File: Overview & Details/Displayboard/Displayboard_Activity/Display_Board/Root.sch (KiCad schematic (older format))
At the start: 38 parts, among them J1 Micro_SD_Card_Det_MOD-Connect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, J2 Conn_01x20_Female, J3 Conn_01x50-Connector_Generic, J4 Conn_01x20_Female, Q1 MMBT2222A-TP-dk_Transistors-B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, U1 MCP130T-300I_TT-dk_PMIC-Super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, U2 SN74LVC245AN-dk_Logic-Buffers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, U3 STMPE811QTR-Interface_Expansi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, U4 SN74LVC245AN-dk_Logic-Buffers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, U5 LP2988-3.3_SOIC8_VSSOP8

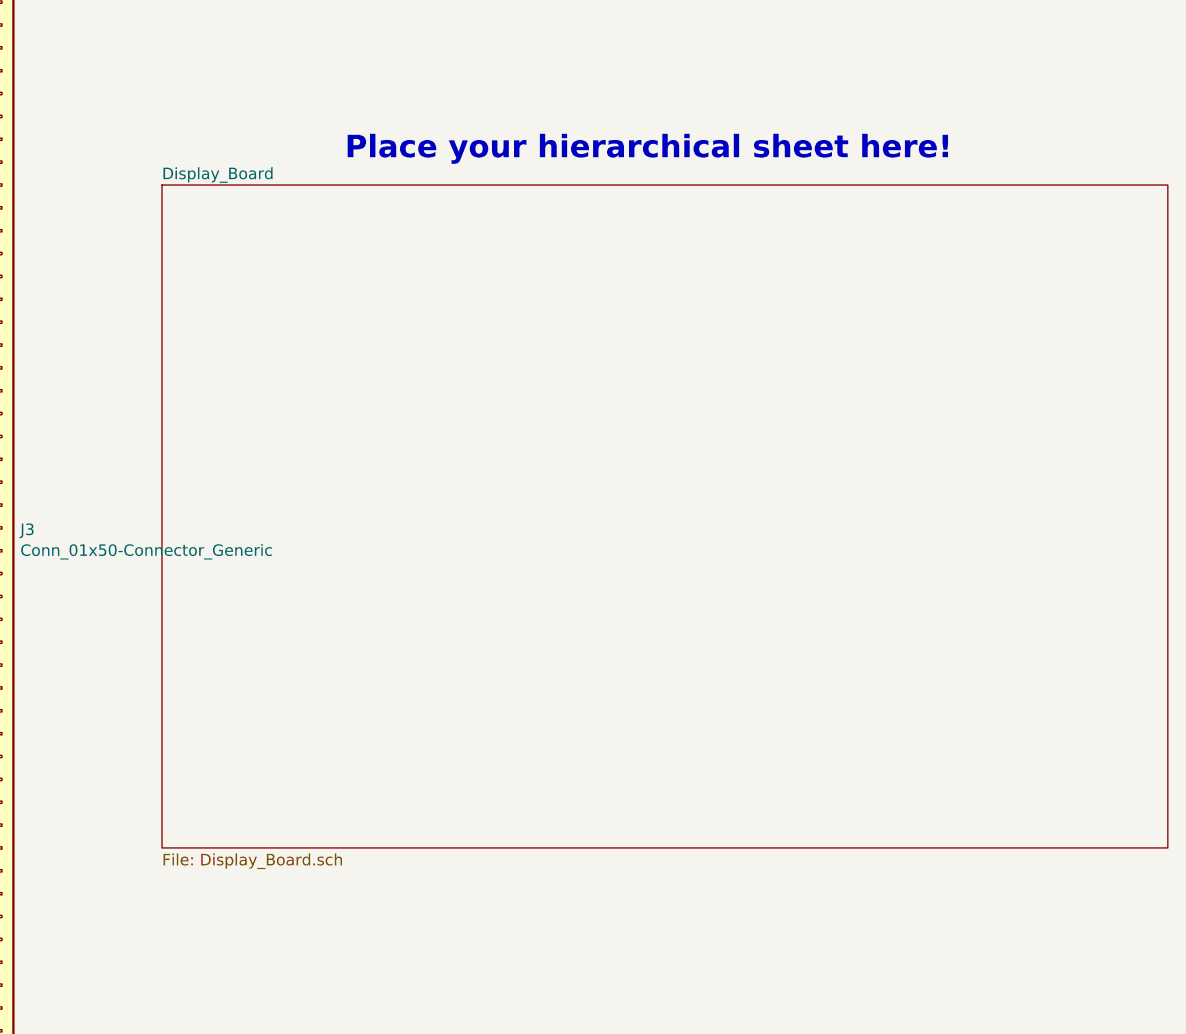
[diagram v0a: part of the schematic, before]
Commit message: Oops removed hierarchical sheet
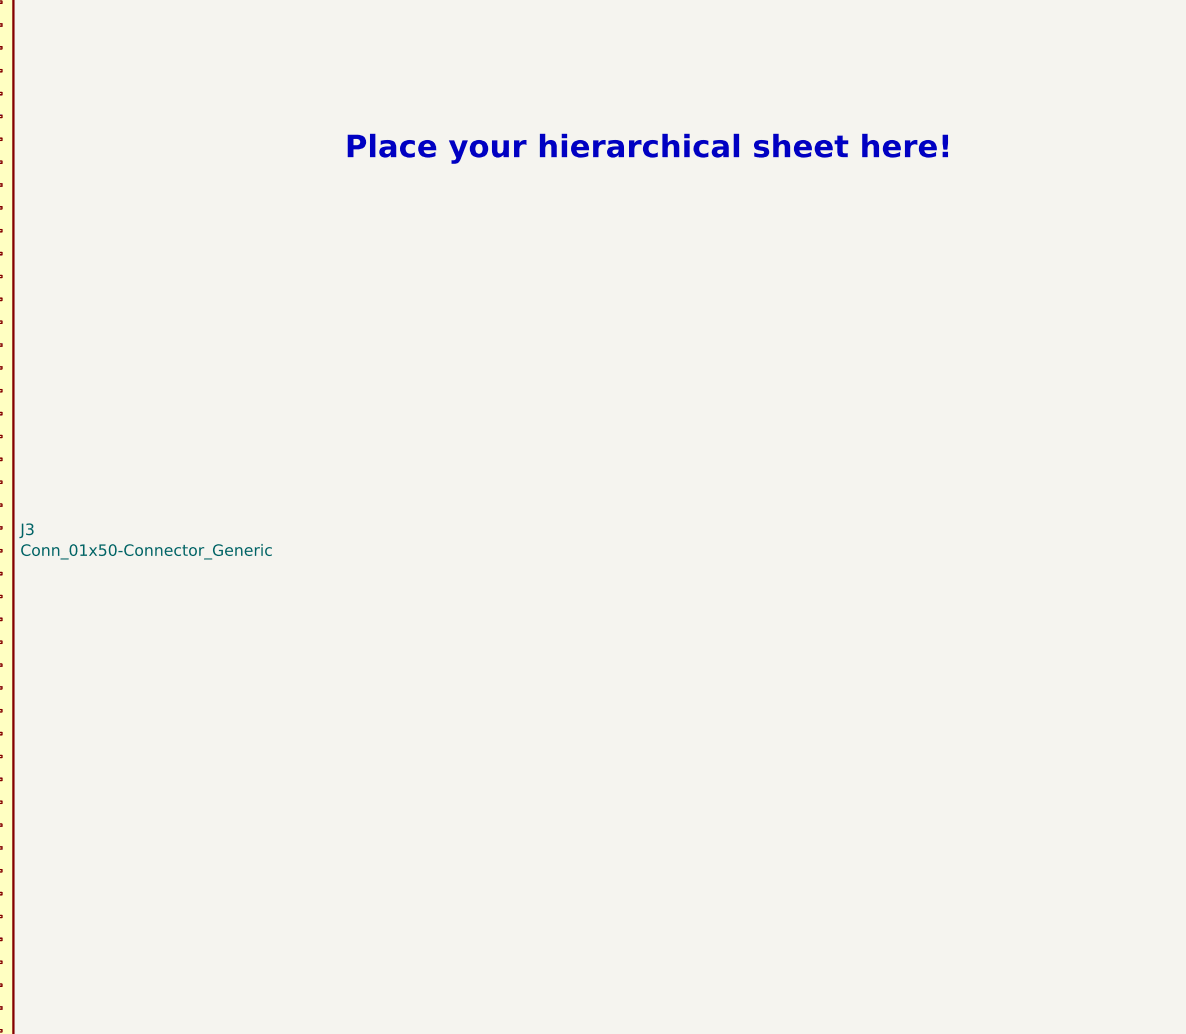
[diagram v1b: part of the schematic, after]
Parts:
- Q1, U1: footprint (none) -> Display_Board:SOT-23-3
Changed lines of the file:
@@
 $Descr B 17000 11000
 encoding utf-8
-Sheet 1 2
+Sheet 1 1
 Title "UberRadio Display Board"
 Date ""
@@
 F 0 "U1" H 4893 7413 60  0000 R CNN
 F 1 "MCP130T-300I_TT-dk_PMIC-Supervisors" H 4893 7307 60  0000 R CNN
-F 2 "" H 5220 7510 60  0001 L CNN
+F 2 "Display_Board:SOT-23-3" H 5220 7510 60  0001 L CNN
 F 3 "http://www.microchip.com/mymicrochip/filehandler.aspx?ddocname=en011325" H 5220 7610 60  0001 L CNN
 F 4 "MCP130T-300I/TTCT-ND" H 5220 7710 60  0001 L CNN "Digi-Key_PN"
@@
 F 0 "Q1" H 9788 2198 60  0000 L CNN
 F 1 "MMBT2222A-TP-dk_Transistors-Bipolar-BJT-Single" H 9788 2092 60  0000 L CNN
-F 2 "" H 9800 2345 60  0001 L CNN
+F 2 "Display_Board:SOT-23-3" H 9800 2345 60  0001 L CNN
 F 3 "http://www.mccsemi.com/up_pdf/MMBT2222A(SOT-23).pdf" H 9800 2445 60  0001 L CNN
 F 4 "MMBT2222ATPMSCT-ND" H 9800 2545 60  0001 L CNN "Digi-Key_PN"
@@
 Text Notes 12650 3750 0    98   ~ 20
 Place your hierarchical sheet here!
-$Sheet
-S 11850 3850 4400 2900
-U 5ED1B308
-F0 "Display_Board" 50
-F1 "Display_Board.sch" 50
-$EndSheet
 $EndSCHEMATC

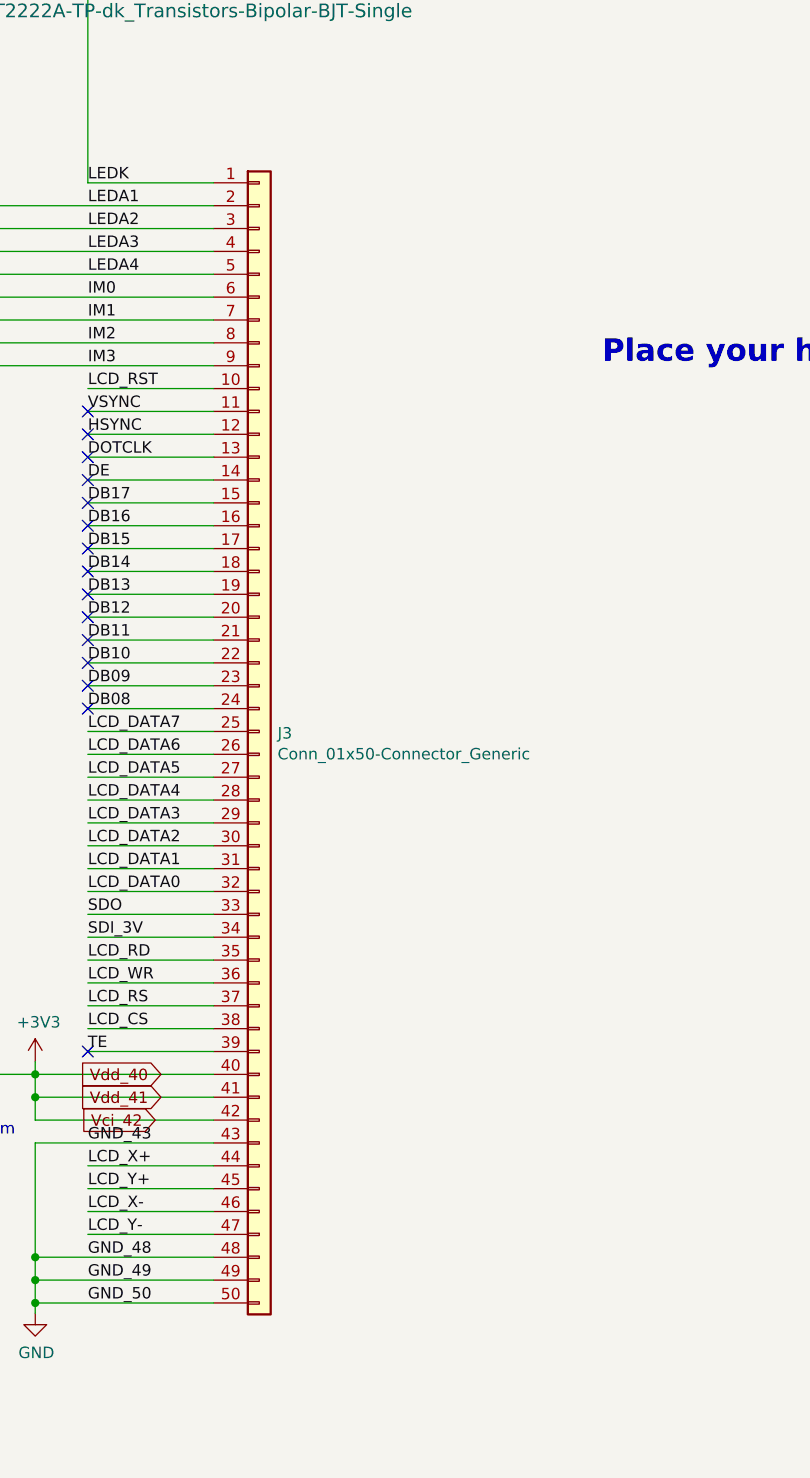
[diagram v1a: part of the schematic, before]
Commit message: Updated with Marion's footprints
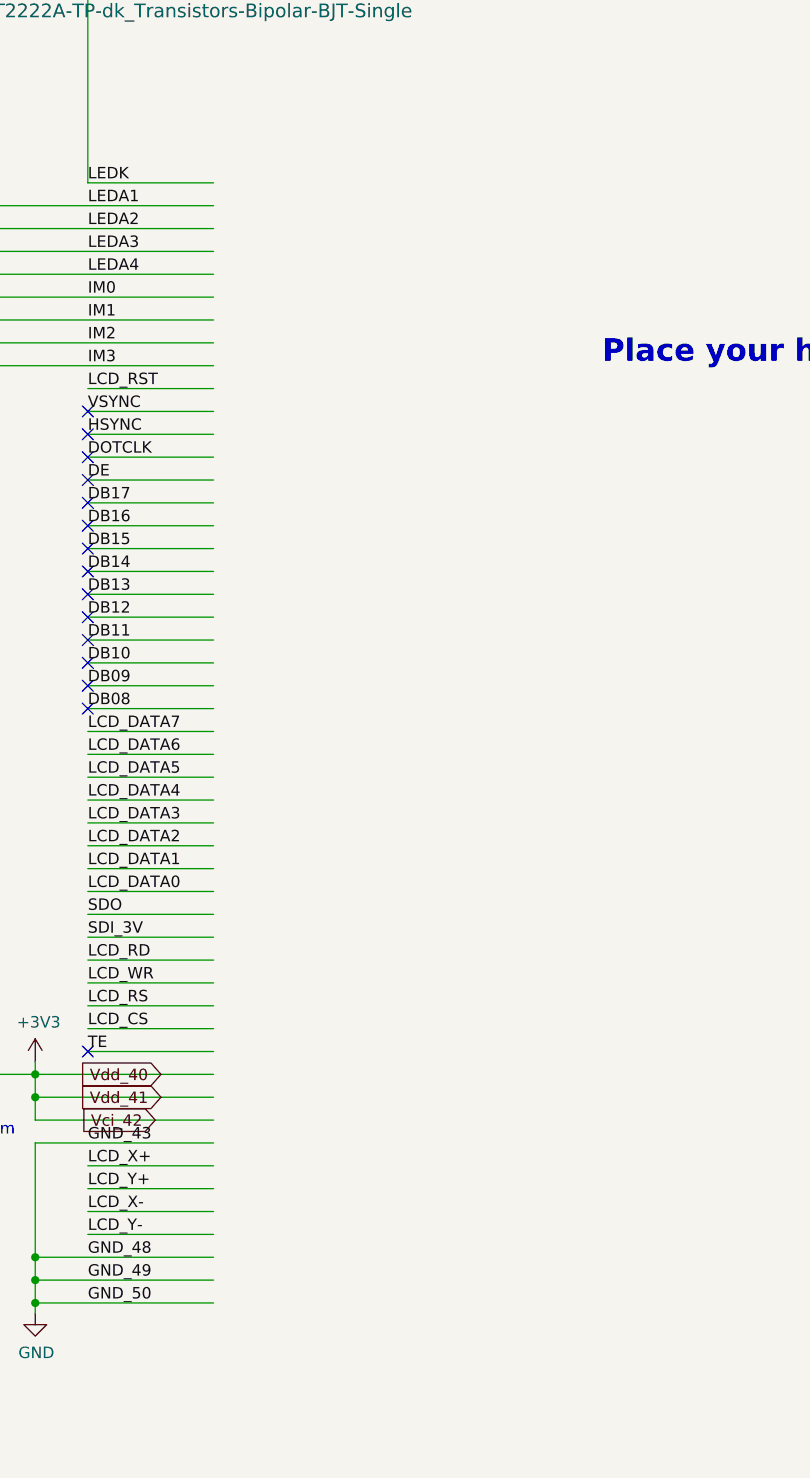
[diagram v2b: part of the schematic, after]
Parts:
- removed J3: Conn_01x50-Connector_Generic, Connector_FFC-FPC:TE_5-1734839-0_1x50-1MP_P0.5mm_Horizontal, symbol Display_Board:Conn_01x50-Connector_Generic
- J2, J4: footprint Connector_PinHeader_2.54mm:PinHeader_1x20_P2.54mm_Vertical -> Display_Board:1X20_ROUND
- JP1, JP2, JP3, JP4: footprint Jumper:SolderJumper-2_P1.3mm_Open_TrianglePad1.0x1.5mm -> Display_Board:SOLDERJUMPER_ARROW_NOPASTE
- U2, U4: footprint (none) -> Display_Board:SN74LVC245ARGYR
- U3: footprint Package_DFN_QFN:QFN-12-1EP_3x3mm_P0.51mm_EP1.45x1.45mm -> Display_Board:STMPE811
- U5: footprint Package_SO:SOIC-8_3.9x4.9mm_P1.27mm -> Display_Board:LP2988IMM-3.3_slash_NOPB
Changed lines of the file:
@@
 F 0 "JP2" V 7950 2860 50  0000 R CNN
 F 1 "SolderJumper_2_Open" V 7805 2822 50  0001 R CNN
-F 2 "Jumper:SolderJumper-2_P1.3mm_Open_TrianglePad1.0x1.5mm" H 7850 2910 50  0001 C CNN
+F 2 "Display_Board:SOLDERJUMPER_ARROW_NOPASTE" H 7850 2910 50  0001 C CNN
 F 3 "~" H 7850 2910 50  0001 C CNN
 	1    7850 2910
@@
 F 0 "JP1" V 7700 2860 50  0000 R CNN
 F 1 "SolderJumper_2_Open" V 7555 2822 50  0001 R CNN
-F 2 "Jumper:SolderJumper-2_P1.3mm_Open_TrianglePad1.0x1.5mm" H 7600 2910 50  0001 C CNN
+F 2 "Display_Board:SOLDERJUMPER_ARROW_NOPASTE" H 7600 2910 50  0001 C CNN
 F 3 "~" H 7600 2910 50  0001 C CNN
 	1    7600 2910
@@
 F 0 "JP3" V 8200 2860 50  0000 R CNN
 F 1 "SolderJumper_2_Open" V 8055 2822 50  0001 R CNN
-F 2 "Jumper:SolderJumper-2_P1.3mm_Open_TrianglePad1.0x1.5mm" H 8100 2910 50  0001 C CNN
+F 2 "Display_Board:SOLDERJUMPER_ARROW_NOPASTE" H 8100 2910 50  0001 C CNN
 F 3 "~" H 8100 2910 50  0001 C CNN
 	1    8100 2910
@@
 F 0 "JP4" V 8450 2860 50  0000 R CNN
 F 1 "SolderJumper_2_Open" V 8305 2822 50  0001 R CNN
-F 2 "Jumper:SolderJumper-2_P1.3mm_Open_TrianglePad1.0x1.5mm" H 8350 2910 50  0001 C CNN
+F 2 "Display_Board:SOLDERJUMPER_ARROW_NOPASTE" H 8350 2910 50  0001 C CNN
 F 3 "~" H 8350 2910 50  0001 C CNN
 	1    8350 2910
@@
 F 0 "U5" H 5280 9522 50  0000 C CNN
 F 1 "LP2988-3.3_SOIC8_VSSOP8" H 5280 9431 50  0000 C CNN
-F 2 "Package_SO:SOIC-8_3.9x4.9mm_P1.27mm" H 5280 9605 50  0001 C CIN
+F 2 "Display_Board:LP2988IMM-3.3_slash_NOPB" H 5280 9605 50  0001 C CIN
 F 3 "http://www.ti.com/lit/ds/symlink/lp2987.pdf" H 5280 9180 50  0001 C CNN
 	1    5280 9180
@@
 F 0 "J2" H 1682 2165 50  0000 C CNN
 F 1 "Conn_01x20_Female" H 1682 2256 50  0000 C CNN
-F 2 "Connector_PinHeader_2.54mm:PinHeader_1x20_P2.54mm_Vertical" H 1790 3390 50  0001 C CNN
+F 2 "Display_Board:1X20_ROUND" H 1790 3390 50  0001 C CNN
 F 3 "~" H 1790 3390 50  0001 C CNN
 	1    1790 3390
@@
 F 0 "J4" H 1687 6160 50  0000 C CNN
 F 1 "Conn_01x20_Female" H 1687 6251 50  0000 C CNN
-F 2 "Connector_PinHeader_2.54mm:PinHeader_1x20_P2.54mm_Vertical" H 1795 7385 50  0001 C CNN
+F 2 "Display_Board:1X20_ROUND" H 1795 7385 50  0001 C CNN
 F 3 "~" H 1795 7385 50  0001 C CNN
 	1    1795 7385
@@
 F 0 "U2" H 5440 5228 60  0000 C CNN
 F 1 "SN74LVC245AN-dk_Logic-Buffers-Drivers-Receivers-Transceivers" H 5440 5122 60  0000 C CNN
-F 2 "" H 5740 4925 60  0001 L CNN
+F 2 "Display_Board:SN74LVC245ARGYR" H 5740 4925 60  0001 L CNN
 F 3 "http://www.ti.com/lit/ds/symlink/sn74lvc245a.pdf" H 5740 5025 60  0001 L CNN
 F 4 "296-8503-5-ND" H 5740 5125 60  0001 L CNN "Digi-Key_PN"
@@
 F 0 "U4" H 8075 5188 60  0000 C CNN
 F 1 "SN74LVC245AN-dk_Logic-Buffers-Drivers-Receivers-Transceivers" H 8075 5082 60  0000 C CNN
-F 2 "" H 8375 4885 60  0001 L CNN
+F 2 "Display_Board:SN74LVC245ARGYR" H 8375 4885 60  0001 L CNN
 F 3 "http://www.ti.com/lit/ds/symlink/sn74lvc245a.pdf" H 8375 4985 60  0001 L CNN
 F 4 "296-8503-5-ND" H 8375 5085 60  0001 L CNN "Digi-Key_PN"
@@
 F 0 "U3" H 7635 8700 50  0000 C CNN
 F 1 "STMPE811QTR-Interface_Expansion" H 7635 8609 50  0000 C CNN
-F 2 "Package_DFN_QFN:QFN-12-1EP_3x3mm_P0.51mm_EP1.45x1.45mm" H 7635 8035 50  0001 C CNN
+F 2 "Display_Board:STMPE811" H 7635 8035 50  0001 C CNN
 F 3 "" H 7635 8035 50  0001 C CNN
 	1    7635 7735
@@
 	1    0    0    -1
 $EndComp
-$Comp
-L Display_Board:Conn_01x50-Connector_Generic J3
-U 1 1 5EDD142B
-P 11150 5350
-F 0 "J3" H 11230 5342 50  0000 L CNN
-F 1 "Conn_01x50-Connector_Generic" H 11230 5251 50  0000 L CNN
-F 2 "Connector_FFC-FPC:TE_5-1734839-0_1x50-1MP_P0.5mm_Horizontal" H 11150 5850 50  0001 C CNN
-F 3 "" H 11150 5850 50  0001 C CNN
-	1    11150 5350
-	1    0    0    -1
-$EndComp
